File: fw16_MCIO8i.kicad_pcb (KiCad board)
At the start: 6 copper layers, 105.4 x 94.3 mm, 112 parts, among them U1 DS160PT801ACBR, U2 TPS62802YKAR, U3 LMQ644A2QRXARQ1

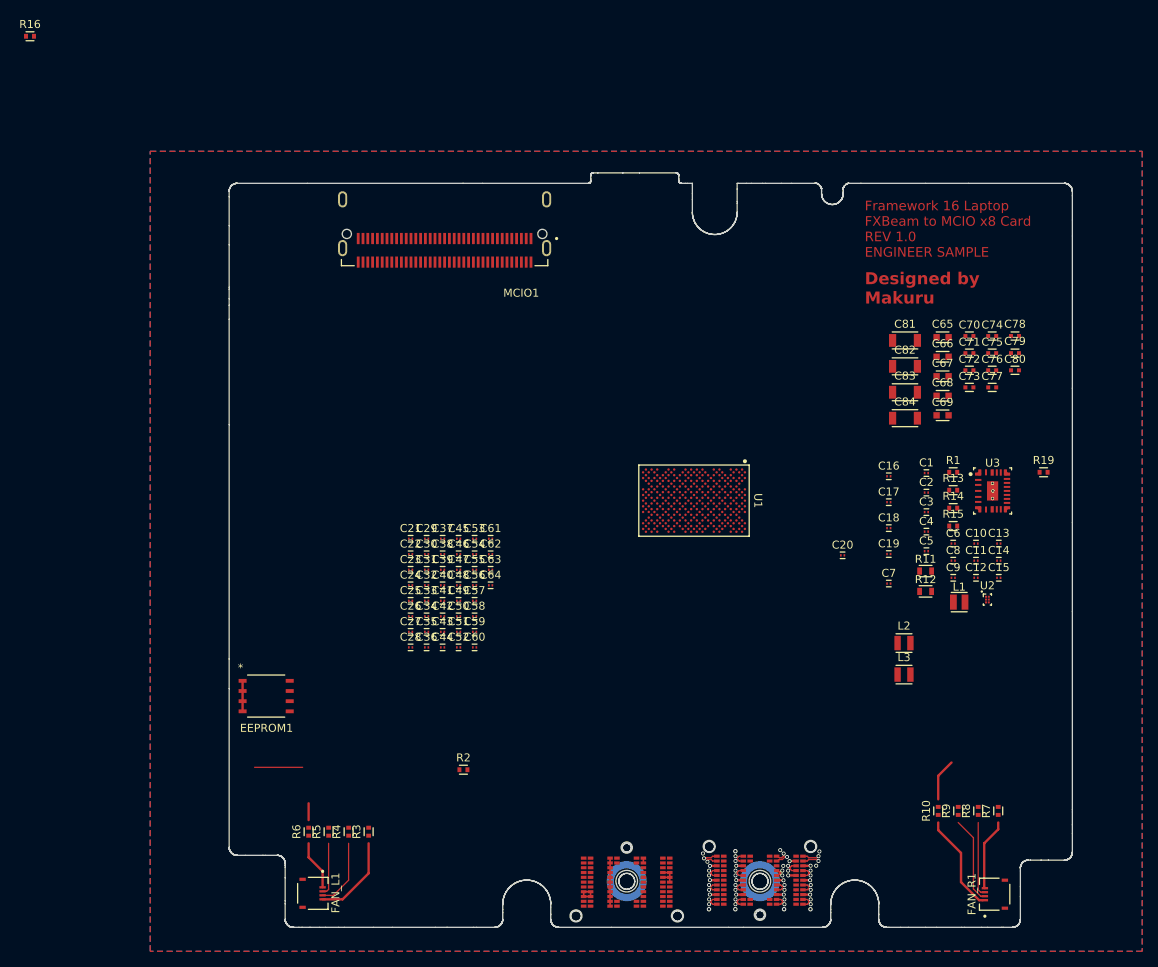
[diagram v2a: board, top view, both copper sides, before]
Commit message: Switch to retimer for only clock
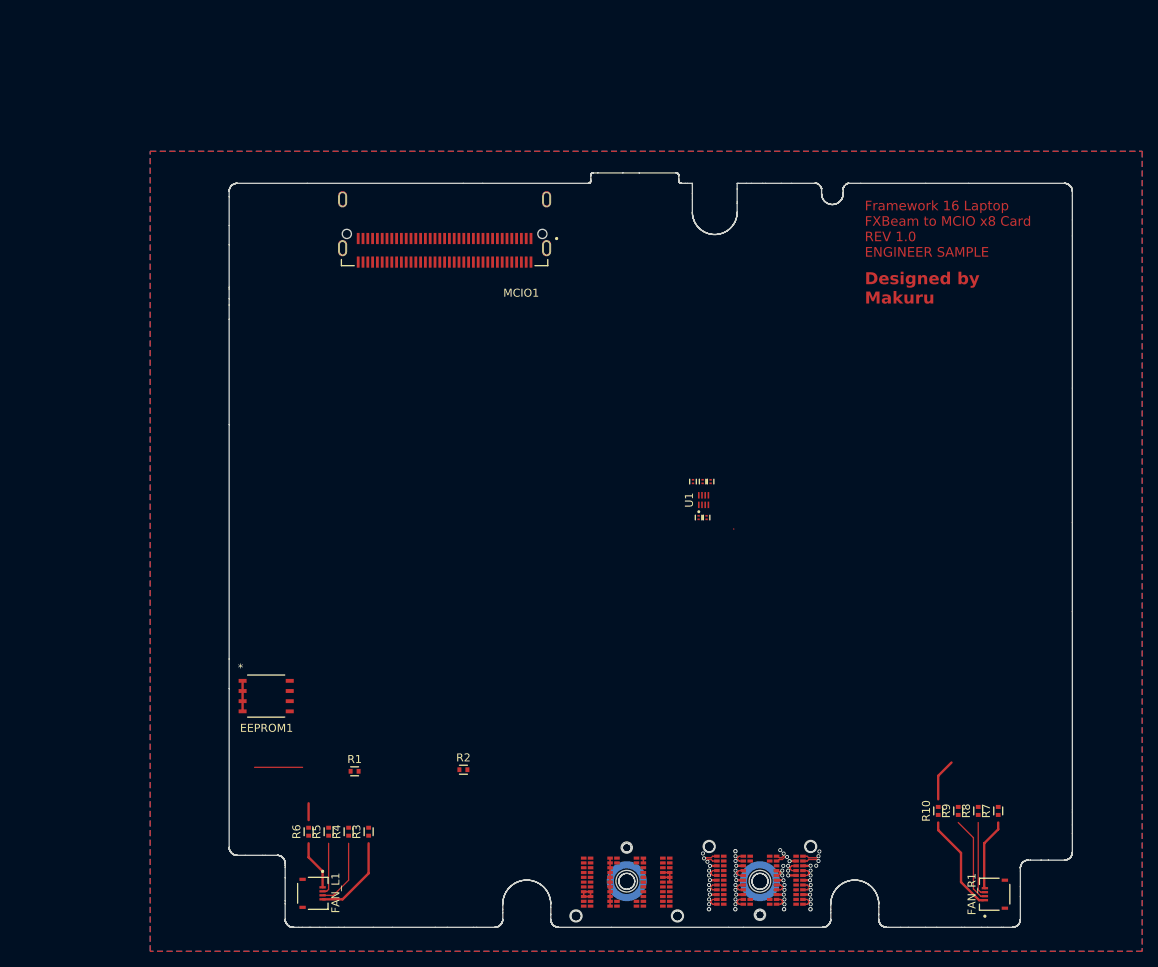
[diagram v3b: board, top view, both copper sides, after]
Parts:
- removed C10, C11, C12, C13, C14, C15, C16, C17, C18, C19, C20, C21, C22, C23, C24, C25, C26, C27, C28, C29, C30, C31, C32, C33, C34, C35, C36, C37, C38, C39, C40, C41, C42, C43, C44, C45, C46, C47, C48, C49, C50, C51, C52, C53, C54, C55, C56, C57, C58, C59, C6, C60, C61, C62, C63, C64, C7, C8, C9: 0201_885012104006, WE_WCAP-CSGP:C_Wurth_WCAP-CSGP-0201
- removed C65, C66, C67, C68, C69: 0603_Fl0.35_R_885012106031, WE_WCAP-CSGP:C_Wurth_WCAP-CSGP-0603_Fl0.35_R
- removed C70, C72, C73: 0402_885012105022, WE_WCAP-CSGP:C_Wurth_WCAP-CSGP-0402
- removed C71, C80: 0402_885012105012, WE_WCAP-CSGP:C_Wurth_WCAP-CSGP-0402
- removed C74, C75: 0402_885012205018, WE_WCAP-CSGP:C_Wurth_WCAP-CSGP-0402
- removed C76: 0402_885012205017, WE_WCAP-CSGP:C_Wurth_WCAP-CSGP-0402
- removed C77: 0402_885012205013, WE_WCAP-CSGP:C_Wurth_WCAP-CSGP-0402
- removed C78: 0402_885392005058, WE_WCAP-CSRF:C_Wurth_WCAP-CSRF-0402
- removed C79: 0402_885392005147, WE_WCAP-CSRF:C_Wurth_WCAP-CSRF-0402
- removed C81, C82, C83, C84: 1206_H1.6_885012208019, WE_WCAP-CSGP:C_Wurth_WCAP-CSGP-1206_H1.6
- removed L1: 2010_744383430047, WE-MAPI:L_Wurth_WE-MAPI-2010
- removed L2, L3: 201610_74479276124, WE-PMCI:L_Wurth_WE-PMCI-201610
- removed R11: 0603_R_560112116007, WE_WRIS-RSKS:R_Wurth_WRIS-RSKS-0603_R
- removed R12: 0603_R_560112116028, WE_WRIS-RSKS:R_Wurth_WRIS-RSKS-0603_R
- removed R13, R15: 0402_560112110019, WE_WRIS-RSKS:R_Wurth_WRIS-RSKS-0402
- removed R14: 0402_560112110012, WE_WRIS-RSKS:R_Wurth_WRIS-RSKS-0402
- removed R16: 0402_560112110215, WE_WRIS-RSKS:R_Wurth_WRIS-RSKS-0402
- removed R19: 0402_560112110088, WE_WRIS-RSKS:R_Wurth_WRIS-RSKS-0402
- removed U2: TPS62802YKAR, step-down-converter-1.8V:YKA0006ACAC
- removed U3: LMQ644A2QRXARQ1, step-down-converter-1.17V:RXA0024A-MFG
- C1, C2, C4, C5: value 0201_885012104006 -> 0201_885012004001
- C3: value 0201_885012104006 -> 0402_885012105020
- R1: value 0402_560112110020 -> 0402_560112110088
- U1: value DS160PT801ACBR -> SY75602ATWL-TR; footprint pcie-redriver:ACB0332A-MFG -> pcie-clk-mux:VDFN8_NNC_MCH
- moved R1 83.6 mm to (41.5, 92.5)
- moved C3 29.4 mm to (83.8, 56.3), turned to -90 degrees
- moved C5 29.3 mm to (85.0, 56.3), turned to 90 degrees
- moved C1 29.0 mm to (84.5, 60.8), turned to -90 degrees
- moved C4 27.7 mm to (86.0, 56.3), turned to 90 degrees
- moved C2 27.7 mm to (85.5, 60.8), turned to -90 degrees
- moved U1 1.20 mm to (85.1, 58.6), turned to 90 degrees
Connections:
- net /fxbeam/PWR.5V renamed /PCIe-clk-mux/PWR.5V
- C1 pad 1: /PCIe_retimer/A_TX.0- -> Net-(U1-IN_P)
- C1 pad 2: unconnected-(C1-Pad2) -> /PCIe-clk-mux/PEX.CLK+
- C2 pad 1: /PCIe_retimer/A_TX.0+ -> Net-(U1-IN_N)
- C2 pad 2: unconnected-(C2-Pad2) -> /PCIe-clk-mux/PEX.CLK-
- C3 pad 1: /PCIe_retimer/A_TX.1- -> /PCIe-clk-mux/PWR.3V3
- C3 pad 2: unconnected-(C3-Pad2) -> Net-(U1-VDD)
- C4 pad 1: /PCIe_retimer/A_TX.1+ -> Net-(U1-OUT1_P)
- C4 pad 2: unconnected-(C4-Pad2) -> /PCIe-clk-mux/PEX_RETIME.CLK+
- C5 pad 1: /PCIe_retimer/A_TX.2- -> /PCIe-clk-mux/PEX_RETIME.CLK-
- C5 pad 2: unconnected-(C5-Pad2) -> Net-(U1-OUT1_N)
- IN1 pad PA4: /fxbeam/PWR.3V3 -> /PCIe-clk-mux/PWR.3V3
- IN1 pad PA5: /fxbeam/PWR.3V3 -> /PCIe-clk-mux/PWR.3V3
- IN1 pad PB4: /fxbeam/PWR.3V3 -> /PCIe-clk-mux/PWR.3V3
- IN1 pad PB5: /fxbeam/PWR.3V3 -> /PCIe-clk-mux/PWR.3V3
- IN1 pad SA1: /PCIe_retimer/A_TX.6+ -> /MCIO/PCI.RX6+
- IN1 pad SA3: /PCIe_retimer/A_TX.4+ -> /MCIO/PCI.RX4+
- IN1 pad SA6: /PCIe_retimer/A_TX.3- -> /MCIO/PCI.RX3-
- IN1 pad SA8: /PCIe_retimer/A_TX.1- -> /MCIO/PCI.RX1-
- IN1 pad SB1: /PCIe_retimer/A_TX.6- -> /MCIO/PCI.RX6-
- IN1 pad SB3: /PCIe_retimer/A_TX.4- -> /MCIO/PCI.RX4-
- IN1 pad SB6: /PCIe_retimer/A_TX.3+ -> /MCIO/PCI.RX3+
- IN1 pad SB8: /PCIe_retimer/A_TX.1+ -> /MCIO/PCI.RX1+
- IN1 pad SC2: /fxbeam/PEX.CLK+ -> /PCIe-clk-mux/PEX.CLK+
- IN1 pad SD1: /PCIe_retimer/A_TX.7- -> /MCIO/PCI.RX7-
- IN1 pad SD2: /fxbeam/PEX.CLK- -> /PCIe-clk-mux/PEX.CLK-
- IN1 pad SD3: /PCIe_retimer/A_TX.5+ -> /MCIO/PCI.RX5+
- IN1 pad SD6: /PCIe_retimer/A_TX.2- -> /MCIO/PCI.RX2-
- IN1 pad SD8: /PCIe_retimer/A_TX.0- -> /MCIO/PCI.RX0-
- IN1 pad SE1: /PCIe_retimer/A_TX.7+ -> /MCIO/PCI.RX7+
- IN1 pad SE3: /PCIe_retimer/A_TX.5- -> /MCIO/PCI.RX5-
- IN1 pad SE6: /PCIe_retimer/A_TX.2+ -> /MCIO/PCI.RX2+
- IN1 pad SE8: /PCIe_retimer/A_TX.0+ -> /MCIO/PCI.RX0+
- IN1 pad SG1: /PCIe_retimer/A_RX.7- -> /MCIO/PCI.TX7-
- IN1 pad SG3: /PCIe_retimer/A_RX.5- -> /MCIO/PCI.TX5-
- IN1 pad SG6: /PCIe_retimer/A_RX.2+ -> /MCIO/PCI.TX2+
- IN1 pad SG8: /PCIe_retimer/A_RX.0- -> /MCIO/PCI.TX0-
- IN1 pad SH1: /PCIe_retimer/A_RX.7+ -> /MCIO/PCI.TX7+
- IN1 pad SH3: /PCIe_retimer/A_RX.5+ -> /MCIO/PCI.TX5+
- IN1 pad SH6: /PCIe_retimer/A_RX.2- -> /MCIO/PCI.TX2-
- IN1 pad SH8: /PCIe_retimer/A_RX.0+ -> /MCIO/PCI.TX0+
- IN1 pad SK1: /PCIe_retimer/A_RX.6+ -> /MCIO/PCI.TX6+
- IN1 pad SK3: /PCIe_retimer/A_RX.4+ -> /MCIO/PCI.TX4+
- IN1 pad SK6: /PCIe_retimer/A_RX.3- -> /MCIO/PCI.TX3-
- IN1 pad SK8: /PCIe_retimer/A_RX.1- -> /MCIO/PCI.TX1-
- IN1 pad SL1: /PCIe_retimer/A_RX.6- -> /MCIO/PCI.TX6-
- IN1 pad SL3: /PCIe_retimer/A_RX.4- -> /MCIO/PCI.TX4-
- IN1 pad SL6: /PCIe_retimer/A_RX.3+ -> /MCIO/PCI.TX3+
- IN1 pad SL8: /PCIe_retimer/A_RX.1+ -> /MCIO/PCI.TX1+
- MCIO1 pad A11: /MCIO/PEXOUT.CLK+ -> /PCIe-clk-mux/PEX_RETIME.CLK+
- MCIO1 pad A12: /MCIO/PEXOUT.CLK- -> /PCIe-clk-mux/PEX_RETIME.CLK-
- MCIO1 pad A14: /MCIO/B_TX.2+ -> /MCIO/PCI.RX2-
- MCIO1 pad A15: /MCIO/B_TX.2- -> /MCIO/PCI.RX2+
- MCIO1 pad A17: /MCIO/B_TX.3+ -> /MCIO/PCI.RX3-
- MCIO1 pad A18: /MCIO/B_TX.3- -> /MCIO/PCI.RX3+
- MCIO1 pad A2: /MCIO/B_TX.0+ -> /MCIO/PCI.RX0-
- MCIO1 pad A20: /MCIO/B_TX.4+ -> /MCIO/PCI.RX4-
- MCIO1 pad A21: /MCIO/B_TX.4- -> /MCIO/PCI.RX4+
- MCIO1 pad A23: /MCIO/B_TX.5+ -> /MCIO/PCI.RX5-
- MCIO1 pad A24: /MCIO/B_TX.5- -> /MCIO/PCI.RX5+
- MCIO1 pad A3: /MCIO/B_TX.0- -> /MCIO/PCI.RX0+
- MCIO1 pad A32: /MCIO/B_TX.6+ -> /MCIO/PCI.RX6-
- MCIO1 pad A33: /MCIO/B_TX.6- -> /MCIO/PCI.RX6+
- MCIO1 pad A35: /MCIO/B_TX.7+ -> /MCIO/PCI.RX7-
- MCIO1 pad A36: /MCIO/B_TX.7- -> /MCIO/PCI.RX7+
- MCIO1 pad A5: /MCIO/B_TX.1+ -> /MCIO/PCI.RX1-
- MCIO1 pad A6: /MCIO/B_TX.1- -> /MCIO/PCI.RX1+
- MCIO1 pad B14: /MCIO/B_RX.2+ -> /MCIO/PCI.TX2-
- MCIO1 pad B15: /MCIO/B_RX.2- -> /MCIO/PCI.TX2+
- MCIO1 pad B17: /MCIO/B_RX.3+ -> /MCIO/PCI.TX3-
- MCIO1 pad B18: /MCIO/B_RX.3- -> /MCIO/PCI.TX3+
- MCIO1 pad B2: /MCIO/B_RX.0+ -> /MCIO/PCI.TX0-
- MCIO1 pad B20: /MCIO/B_RX.4+ -> /MCIO/PCI.TX4-
- MCIO1 pad B21: /MCIO/B_RX.4- -> /MCIO/PCI.TX4+
- MCIO1 pad B23: /MCIO/B_RX.5+ -> /MCIO/PCI.TX5-
- MCIO1 pad B24: /MCIO/B_RX.5- -> /MCIO/PCI.TX5+
- MCIO1 pad B3: /MCIO/B_RX.0- -> /MCIO/PCI.TX0+
- MCIO1 pad B32: /MCIO/B_RX.6+ -> /MCIO/PCI.TX6-
- MCIO1 pad B33: /MCIO/B_RX.6- -> /MCIO/PCI.TX6+
- MCIO1 pad B35: /MCIO/B_RX.7+ -> /MCIO/PCI.TX7-
- MCIO1 pad B36: /MCIO/B_RX.7- -> /MCIO/PCI.TX7+
- MCIO1 pad B5: /MCIO/B_RX.1+ -> /MCIO/PCI.TX1-
- MCIO1 pad B6: /MCIO/B_RX.1- -> /MCIO/PCI.TX1+
- MCIO1 pad B8: unconnected-(MCIO1-SM_SCL-PadB8) -> /MCIO/PEX.SCL
- MCIO1 pad B9: unconnected-(MCIO1-SM_SDA-PadB9) -> /MCIO/PEX.SDA
- R1 pad 2: GND -> Net-(IN1-ID1)
- R2 pad 2: Net-(IN1-ID1) -> Net-(IN1-ID0)
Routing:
- net /PCIe_retimer/A_RX.5+: track 41.6 -> 0.00 mm, vias 1 -> 0
- net /MCIO/PCI.TX5+: track 0.00 -> 41.6 mm, vias 0 -> 1
- net /PCIe_retimer/A_RX.5-: track 41.0 -> 0.00 mm, vias 1 -> 0
- net /MCIO/PCI.TX5-: track 0.00 -> 41.0 mm, vias 0 -> 1
- net /PCIe_retimer/A_RX.1+: track 25.3 -> 0.00 mm, vias 1 -> 0
- net /MCIO/PCI.TX1+: track 0.00 -> 25.3 mm, vias 0 -> 1
- net /PCIe_retimer/A_RX.1-: track 24.7 -> 0.00 mm, vias 1 -> 0
- net /MCIO/PCI.TX1-: track 0.00 -> 24.7 mm, vias 0 -> 1
- net /PCIe_retimer/A_RX.0+: track 24.1 -> 0.00 mm, vias 1 -> 0
- net /MCIO/PCI.TX0+: track 0.00 -> 24.1 mm, vias 0 -> 1
- net /PCIe_retimer/A_RX.0-: track 23.5 -> 0.00 mm, vias 1 -> 0
- net /MCIO/PCI.TX0-: track 0.00 -> 23.5 mm, vias 0 -> 1
- net /PCIe_retimer/A_TX.0+: track 18.2 -> 0.00 mm, vias 1 -> 0
- net /MCIO/PCI.RX0+: track 0.00 -> 18.2 mm, vias 0 -> 1
- net /PCIe_retimer/A_TX.0-: track 17.7 -> 0.00 mm, vias 1 -> 0
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
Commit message: Fixed board dimensions
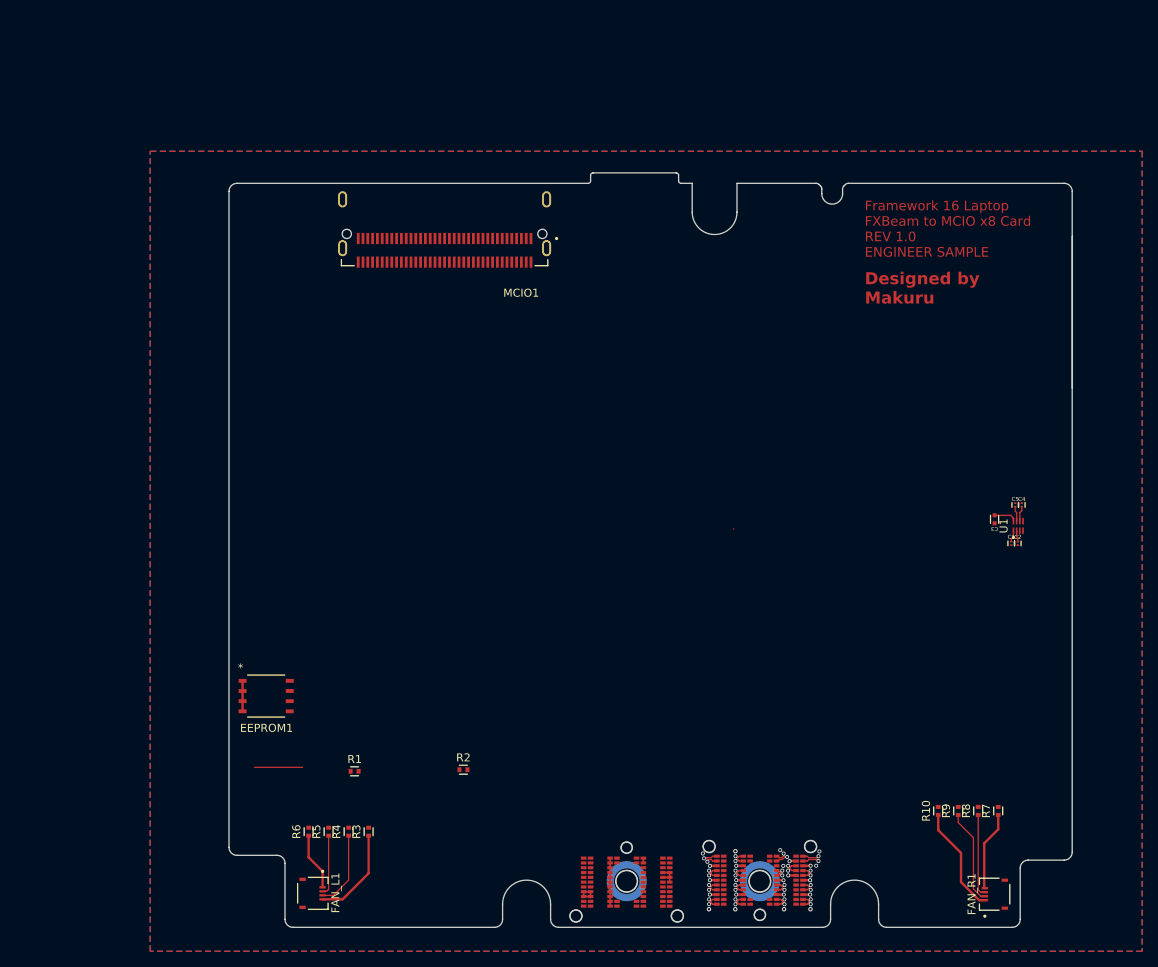
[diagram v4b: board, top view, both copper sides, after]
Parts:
- C3: footprint WE_WCAP-CSGP:C_Wurth_WCAP-CSGP-0201 -> WE_WCAP-CSGP:C_Wurth_WCAP-CSGP-0402
- moved U1 39.5 mm to (124.5, 61.8)
- moved C1 39.2 mm to (123.6, 64.0)
- moved C5 39.2 mm to (124.1, 59.2)
- moved C2 39.0 mm to (124.4, 64.0)
- moved C4 39.0 mm to (124.9, 59.2)
- moved C3 38.0 mm to (121.5, 61.0), turned to 90 degrees
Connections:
- net /PCIe-clk-mux/PEX_RETIME.CLK+ renamed /MCIO/PEX_RETIME.CLK+
- C5 pad 1: /PCIe-clk-mux/PEX_RETIME.CLK- -> Net-(U1-OUT1_N)
- C5 pad 2: Net-(U1-OUT1_N) -> /MCIO/PEX_RETIME.CLK-
- IN1 pad PK1: /fxbeam/PEX.SCL -> /MCIO/PEX.SCL
- IN1 pad PL2: /fxbeam/PEX.SDA -> /MCIO/PEX.SDA
- MCIO1 pad A12: /PCIe-clk-mux/PEX_RETIME.CLK- -> /MCIO/PEX_RETIME.CLK-
- MCIO1 pad B11: unconnected-(MCIO1-PERST-PadB11) -> /fxbeam/PEX.RST
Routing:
- net (no net): track 7.42 -> 0.04 mm
- net Net-(U1-VDD): track 0.00 -> 2.88 mm
- net Net-(U1-OUT1_P): track 0.00 -> 1.91 mm
- net Net-(U1-OUT1_N): track 0.00 -> 1.88 mm
- net Net-(U1-IN_P): track 0.00 -> 1.48 mm
- net Net-(U1-IN_N): track 0.00 -> 1.43 mm
- net Net-(FAN_R1-Pad1): track 12.3 -> 13.3 mm
- net Net-(FAN_R1-Pad4): track 8.97 -> 9.92 mm
- net Net-(FAN_R1-Pad3): track 9.24 -> 10.2 mm
- net Net-(FAN_R1-Pad2): track 10.8 -> 11.7 mm
- net Net-(FAN_L1-Pad4): track 10.8 -> 11.8 mm
- net Net-(FAN_L1-Pad3): track 8.64 -> 9.59 mm
- net Net-(FAN_L1-Pad2): track 6.61 -> 7.56 mm
- net Net-(FAN_L1-Pad1): track 6.22 -> 7.17 mm
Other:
- outline, holes or cut-outs redrawn

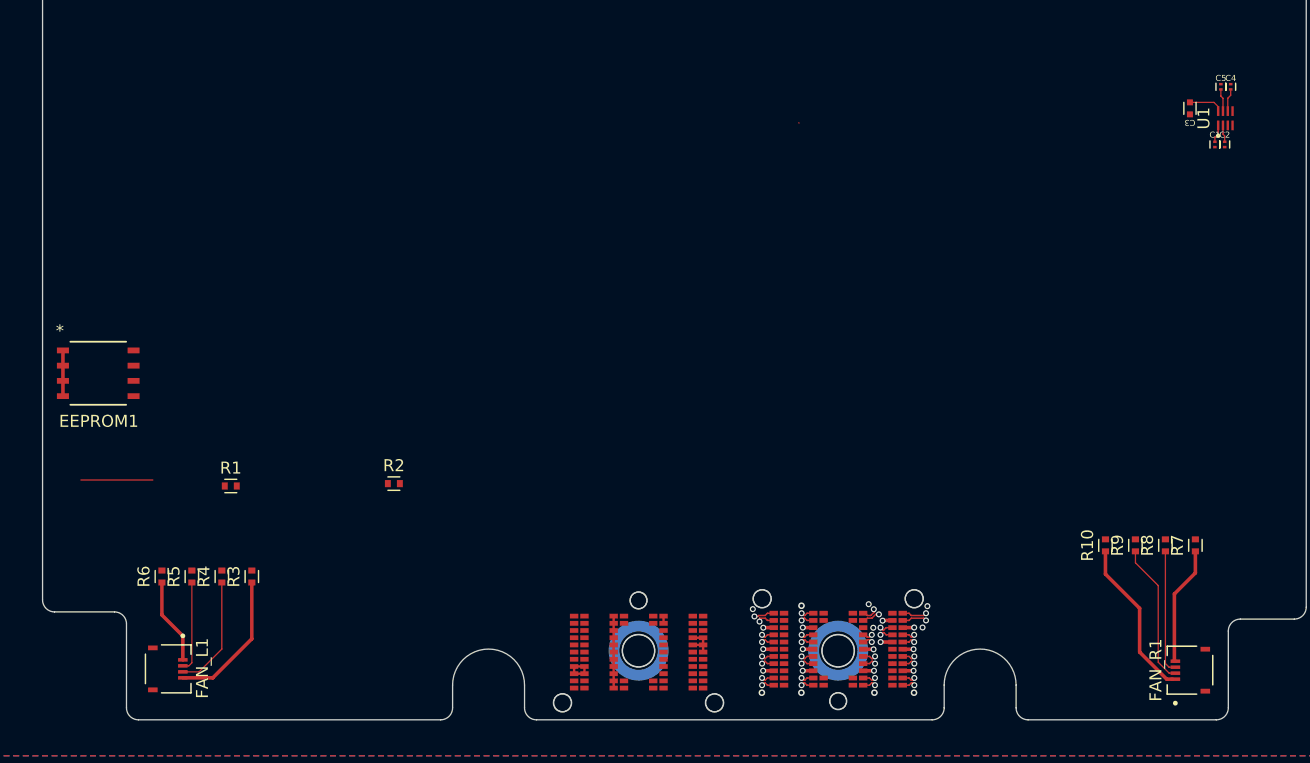
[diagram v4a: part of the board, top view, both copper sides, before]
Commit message: Fixed board stackup
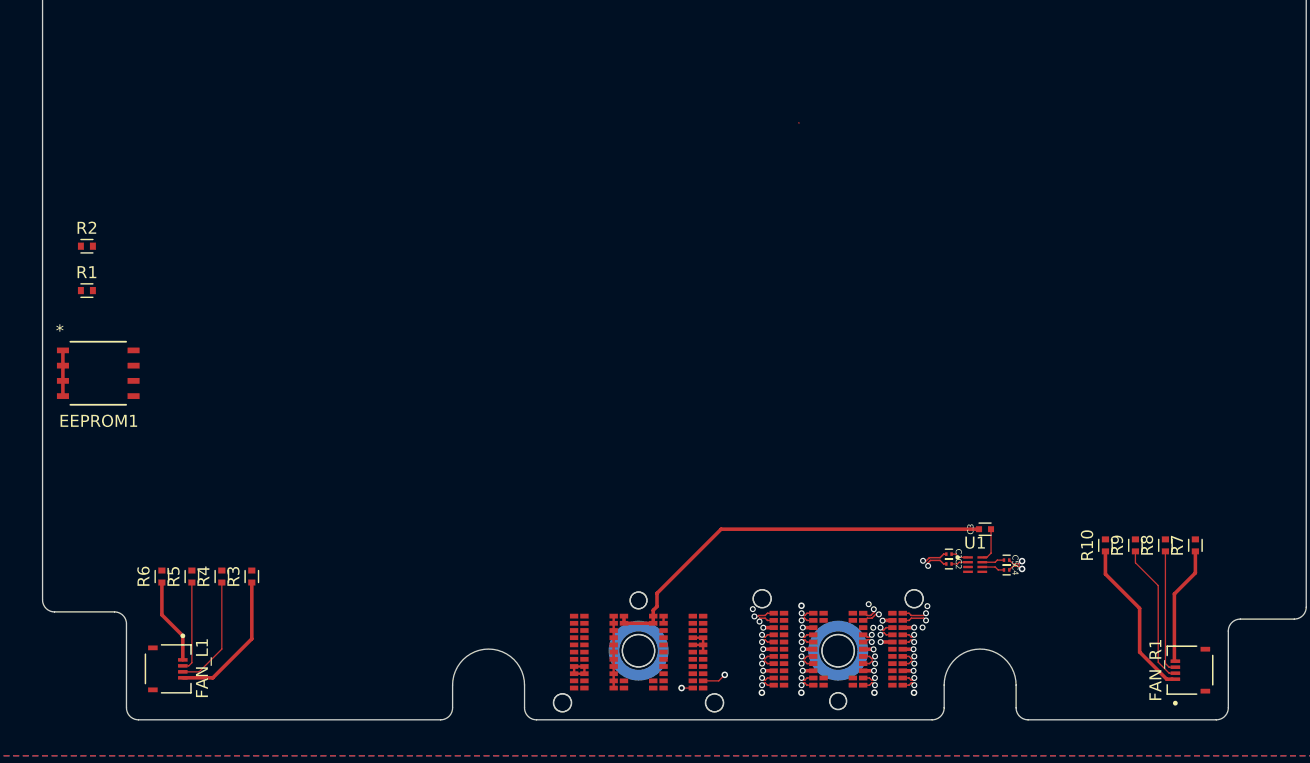
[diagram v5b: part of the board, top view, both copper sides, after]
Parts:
- moved C4 44.4 mm to (106.2, 99.5), turned to 0 degrees
- moved C5 43.3 mm to (106.2, 98.7), turned to 0 degrees
- moved U1 42.7 mm to (103.6, 99.1), turned to 0 degrees
- moved C2 41.9 mm to (101.4, 99.0), turned to 180 degrees
- moved C1 40.7 mm to (101.4, 98.2), turned to 180 degrees
- moved C3 39.0 mm to (104.4, 96.1), turned to 0 degrees
- moved R2 32.4 mm to (29.5, 72.5)
- moved R1 20.2 mm to (29.5, 76.2)
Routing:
- net /PCIe-clk-mux/PWR.3V3: track 0.00 -> 34.7 mm
- net /MCIO/PEX.SCL: track 0.00 -> 6.89 mm, vias 0 -> 1
- net Net-(IN1-ID1): track 6.00 -> 0.00 mm
- net /MCIO/PEX.SDA: track 0.00 -> 4.39 mm, vias 0 -> 1
- net /PCIe-clk-mux/PEX.CLK+: track 6.85 -> 11.1 mm, vias 1 -> 2
- net /PCIe-clk-mux/PEX.CLK-: track 7.04 -> 11.1 mm, vias 1 -> 2
- net /MCIO/PEX_RETIME.CLK-: track 0.00 -> 1.29 mm, vias 0 -> 1
- net /MCIO/PEX_RETIME.CLK+: track 0.00 -> 1.29 mm, vias 0 -> 1

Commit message: Routing
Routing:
- net /MCIO/PCI.TX5+: track 41.6 -> 13.9 mm
- net /MCIO/PCI.TX5-: track 41.0 -> 13.7 mm
- net GND: track 28.0 -> 16.3 mm, vias 23 -> 38
- net /MCIO/PCI.TX3-: track 16.9 -> 26.3 mm
- net /MCIO/PCI.TX3+: track 17.4 -> 26.8 mm
- net /MCIO/PCI.TX4-: track 13.4 -> 20.3 mm
- net /MCIO/PCI.TX4+: track 13.2 -> 19.8 mm
- net /MCIO/PCI.RX7+: track 10.7 -> 5.58 mm
- net /MCIO/PCI.TX0+: track 24.1 -> 19.0 mm
- net /MCIO/PCI.TX0-: track 23.5 -> 18.4 mm
- net /MCIO/PCI.RX7-: track 10.4 -> 5.41 mm
- net /MCIO/PCI.TX1+: track 25.3 -> 20.9 mm
- net /MCIO/PCI.TX1-: track 24.7 -> 20.3 mm
- net /MCIO/PCI.RX4-: track 11.2 -> 7.95 mm
- net /MCIO/PCI.RX4+: track 10.9 -> 7.74 mm
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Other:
- outline, holes or cut-outs redrawn

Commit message: Routing small schematic fix
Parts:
- moved C1 0.29 mm to (101.1, 98.2)
- moved C2 0.29 mm to (101.1, 99.0)
- moved C4 0.15 mm to (106.1, 99.5)
- moved C5 0.15 mm to (106.1, 98.6)
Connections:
- C1 pad 1: Net-(U1-IN_P) -> /PCIe-clk-mux/CLK+
- C2 pad 1: Net-(U1-IN_N) -> /PCIe-clk-mux/CLK-
- C4 pad 1: Net-(U1-OUT1_P) -> /PCIe-clk-mux/CLK+
- C5 pad 1: Net-(U1-OUT1_N) -> /PCIe-clk-mux/CLK-
- U1 pad 1: Net-(U1-IN_P) -> /PCIe-clk-mux/CLK+
- U1 pad 2: Net-(U1-IN_N) -> /PCIe-clk-mux/CLK-
- U1 pad 6: Net-(U1-OUT1_P) -> /PCIe-clk-mux/CLK+
- U1 pad 7: Net-(U1-OUT1_N) -> /PCIe-clk-mux/CLK-
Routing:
- net /MCIO/PCI.TX7+: track 7.25 -> 16.0 mm, vias 1 -> 2
- net /MCIO/PCI.TX6-: track 8.57 -> 17.3 mm, vias 1 -> 2
- net /MCIO/PCI.TX7-: track 7.08 -> 15.6 mm, vias 1 -> 2
- net /MCIO/PCI.TX6+: track 8.39 -> 16.9 mm, vias 1 -> 2
- net /MCIO/PCI.RX7+: track 5.58 -> 13.4 mm, vias 1 -> 2
- net /MCIO/PCI.RX6-: track 4.78 -> 12.5 mm, vias 1 -> 2
- net /MCIO/PCI.RX7-: track 5.41 -> 13.0 mm, vias 1 -> 2
- net /MCIO/PCI.RX6+: track 4.60 -> 12.1 mm, vias 1 -> 2
- net /MCIO/PEX_RETIME.CLK+: track 1.29 -> 6.33 mm, vias 1 -> 2
- net /MCIO/PEX_RETIME.CLK-: track 1.29 -> 5.99 mm, vias 1 -> 2
- net /PCIe-clk-mux/CLK+: track 0.00 -> 3.64 mm
- net /PCIe-clk-mux/CLK-: track 0.00 -> 3.63 mm
- net Net-(U1-OUT1_P): track 1.91 -> 0.00 mm
- net Net-(U1-OUT1_N): track 1.88 -> 0.00 mm
- net /MCIO/PCI.RX2+: track 14.4 -> 16.2 mm, vias 1 -> 2
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
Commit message: Routing
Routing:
- net /MCIO/PEX_RETIME.CLK-: track 5.99 -> 122.6 mm
- net /MCIO/PEX_RETIME.CLK+: track 6.33 -> 122.2 mm
- net /MCIO/PCI.TX5+: track 12.6 -> 13.1 mm
- net GND: vias 88 -> 84
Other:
- board text added: "Framework 16 Laptop FXBeam to MCIO x8 Card REV 1.1 ENGINEER SAMPLE"
- board text removed: "Framework 16 Laptop FXBeam to MCIO x8 Card REV 1.0 ENGINEER SAMPLE"
